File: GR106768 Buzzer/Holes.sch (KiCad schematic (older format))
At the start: 105 parts

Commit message: trying to add vias
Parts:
- H1, H10, H100, H101, H102, H103, H104, H105, H11, H12, H13, H14, H15, H16, H17, H18, H19, H2, H20, H21, H22, H23, H24, H25, H26, H27, H28, H29, H3, H30, H31, H32, H33, H34, H35, H36, H37, H38, H39, H4, H40, H41, H42, H43, H44, H45, H46, H47, H48, H49, H5, H50, H51, H52, H53, H54, H55, H56, H57, H58, H59, H6, H60, H61, H62, H63, H64, H65, H66, H67, H68, H69, H7, H70, H71, H72, H73, H74, H75, H76, H77, H78, H79, H8, H80, H81, H82, H83, H84, H85, H86, H87, H88, H89, H9, H90, H91, H92, H93, H94, H95, H96, H97, H98, H99: value Via -> GND

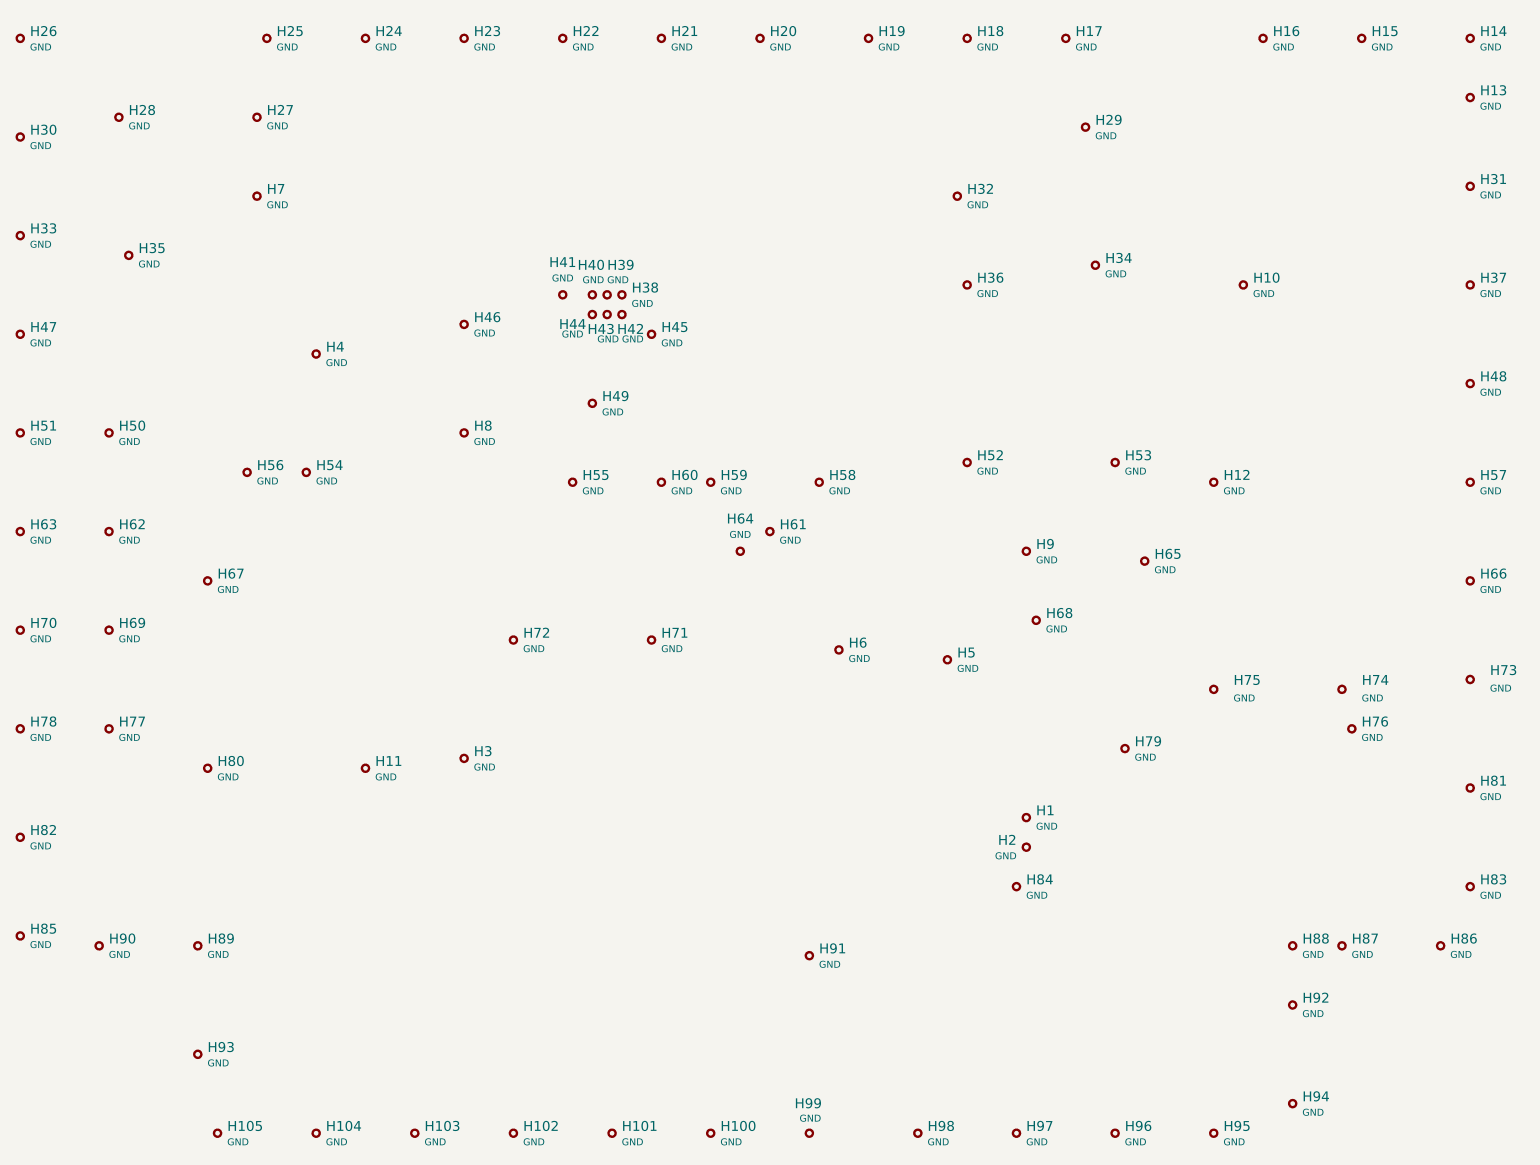
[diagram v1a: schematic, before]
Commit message: buzzer board custom via footprints
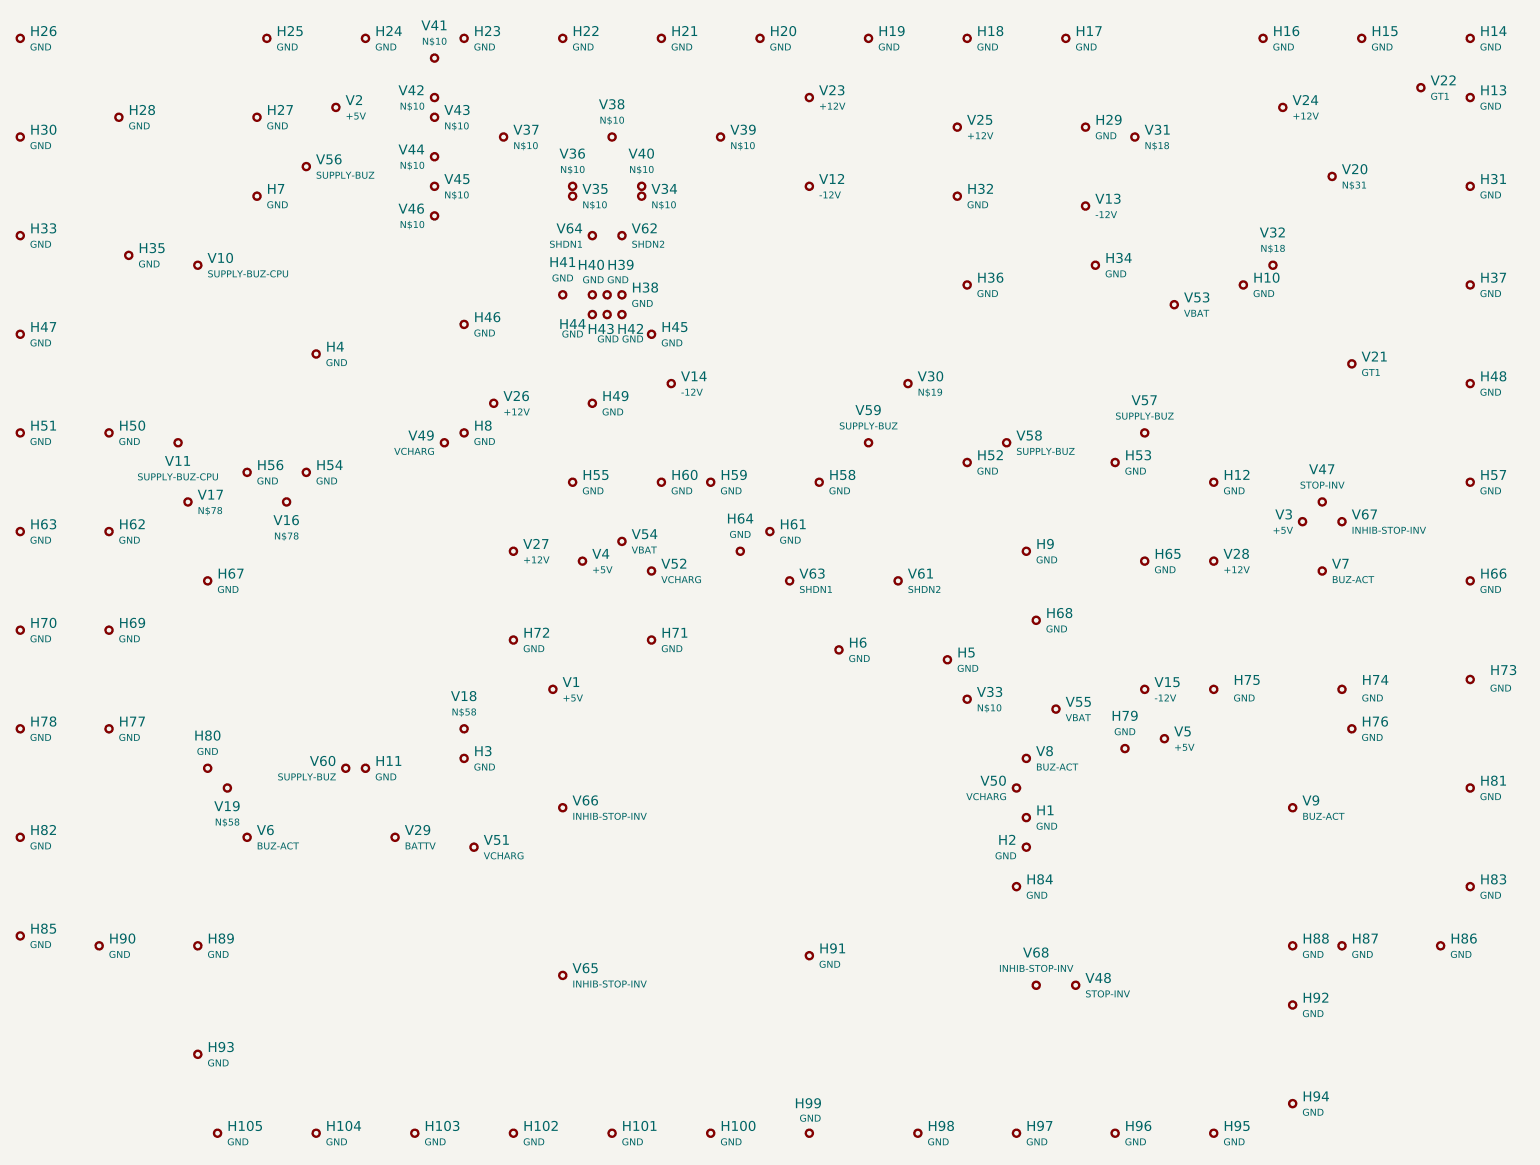
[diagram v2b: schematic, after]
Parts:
- added V1, V2, V3, V4, V5: +5V, AllModules:Via_12x32-1._.3.4, symbol GR106768_Buzzer:Via
- added V10, V11: SUPPLY-BUZ-CPU, AllModules:Via_12x32-1._.3.4, symbol GR106768_Buzzer:Via
- added V12, V13, V14, V15: -12V, AllModules:Via_12x32-1._.3.4, symbol GR106768_Buzzer:Via
- added V16, V17: N$78, AllModules:Via_12x32-1._.3.4, symbol GR106768_Buzzer:Via
- added V18, V19: N$58, AllModules:Via_12x32-1._.3.4, symbol GR106768_Buzzer:Via
- added V20: N$31, AllModules:Via_12x32-1._.3.4, symbol GR106768_Buzzer:Via
- added V21, V22: GT1, AllModules:Via_12x32-1._.3.4, symbol GR106768_Buzzer:Via
- added V23, V24, V25, V26, V27, V28: +12V, AllModules:Via_12x32-1._.3.4, symbol GR106768_Buzzer:Via
- added V29: BATTV, AllModules:Via_12x32-1._._.4, symbol GR106768_Buzzer:Via
- added V30: N$19, AllModules:Via_12x32-1._.3.4, symbol GR106768_Buzzer:Via
- added V31, V32: N$18, AllModules:Via_12x32-1._.3.4, symbol GR106768_Buzzer:Via
- added V33: N$10, AllModules:Via_12x32-1._._.4, symbol GR106768_Buzzer:Via
- added V34, V35, V36, V37, V38, V39, V40, V41, V42, V43, V44, V45, V46: N$10, AllModules:Via_12x32-1._.3.4, symbol GR106768_Buzzer:Via
- added V47, V48: STOP-INV, AllModules:Via_12x32-1._.3.4, symbol GR106768_Buzzer:Via
- added V49, V52: VCHARG, AllModules:Via_12x32-1._._.4, symbol GR106768_Buzzer:Via
- added V50, V51: VCHARG, AllModules:Via_12x32-1._.3.4, symbol GR106768_Buzzer:Via
- added V53, V54, V55: VBAT, AllModules:Via_12x32-1._.3.4, symbol GR106768_Buzzer:Via
- added V56, V57, V58, V59, V60: SUPPLY-BUZ, AllModules:Via_12x32-1._.3.4, symbol GR106768_Buzzer:Via
- added V6, V7, V8, V9: BUZ-ACT, AllModules:Via_12x32-1._.3.4, symbol GR106768_Buzzer:Via
- added V61, V62: SHDN2, AllModules:Via_12x32-1._._.4, symbol GR106768_Buzzer:Via
- added V63, V64: SHDN1, AllModules:Via_12x32-1._._.4, symbol GR106768_Buzzer:Via
- added V65, V66, V67, V68: INHIB-STOP-INV, AllModules:Via_12x32-1._.3.4, symbol GR106768_Buzzer:Via
- H1, H10, H100, H101, H102, H103, H104, H105, H11, H12, H13, H14, H15, H16, H17, H18, H19, H2, H20, H21, H22, H23, H24, H25, H26, H27, H28, H29, H3, H30, H31, H32, H33, H34, H35, H36, H37, H38, H39, H4, H40, H41, H42, H43, H44, H45, H46, H47, H48, H49, H5, H50, H51, H52, H53, H54, H55, H56, H57, H58, H59, H6, H60, H61, H62, H63, H64, H65, H66, H67, H68, H69, H7, H70, H71, H72, H73, H74, H75, H76, H77, H78, H79, H8, H80, H81, H82, H83, H84, H85, H86, H87, H88, H89, H9, H90, H91, H92, H93, H94, H95, H96, H97, H98, H99: footprint AllModules:ThroughHole_60milx12mil_Pad_Cu_Mask -> AllModules:Via_12x32
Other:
- moved on the sheet: H11

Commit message: Added Via from Buzzer board to Mechanical.lib
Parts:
- H1, H10, H100, H101, H102, H103, H104, H105, H11, H12, H13, H14, H15, H16, H17, H18, H19, H2, H20, H21, H22, H23, H24, H25, H26, H27, H28, H29, H3, H30, H31, H32, H33, H34, H35, H36, H37, H38, H39, H4, H40, H41, H42, H43, H44, H45, H46, H47, H48, H49, H5, H50, H51, H52, H53, H54, H55, H56, H57, H58, H59, H6, H60, H61, H62, H63, H64, H65, H66, H67, H68, H69, H7, H70, H71, H72, H73, H74, H75, H76, H77, H78, H79, H8, H80, H81, H82, H83, H84, H85, H86, H87, H88, H89, H9, H90, H91, H92, H93, H94, H95, H96, H97, H98, H99, V1, V10, V11, V12, V13, V14, V15, V16, V17, V18, V19, V2, V20, V21, V22, V23, V24, V25, V26, V27, V28, V29, V3, V30, V31, V32, V33, V34, V35, V36, V37, V38, V39, V4, V40, V41, V42, V43, V44, V45, V46, V47, V48, V49, V5, V50, V51, V52, V53, V54, V55, V56, V57, V58, V59, V6, V60, V61, V62, V63, V64, V65, V66, V67, V68, V7, V8, V9: symbol GR106768_Buzzer:Via -> V_Mechanical:Via

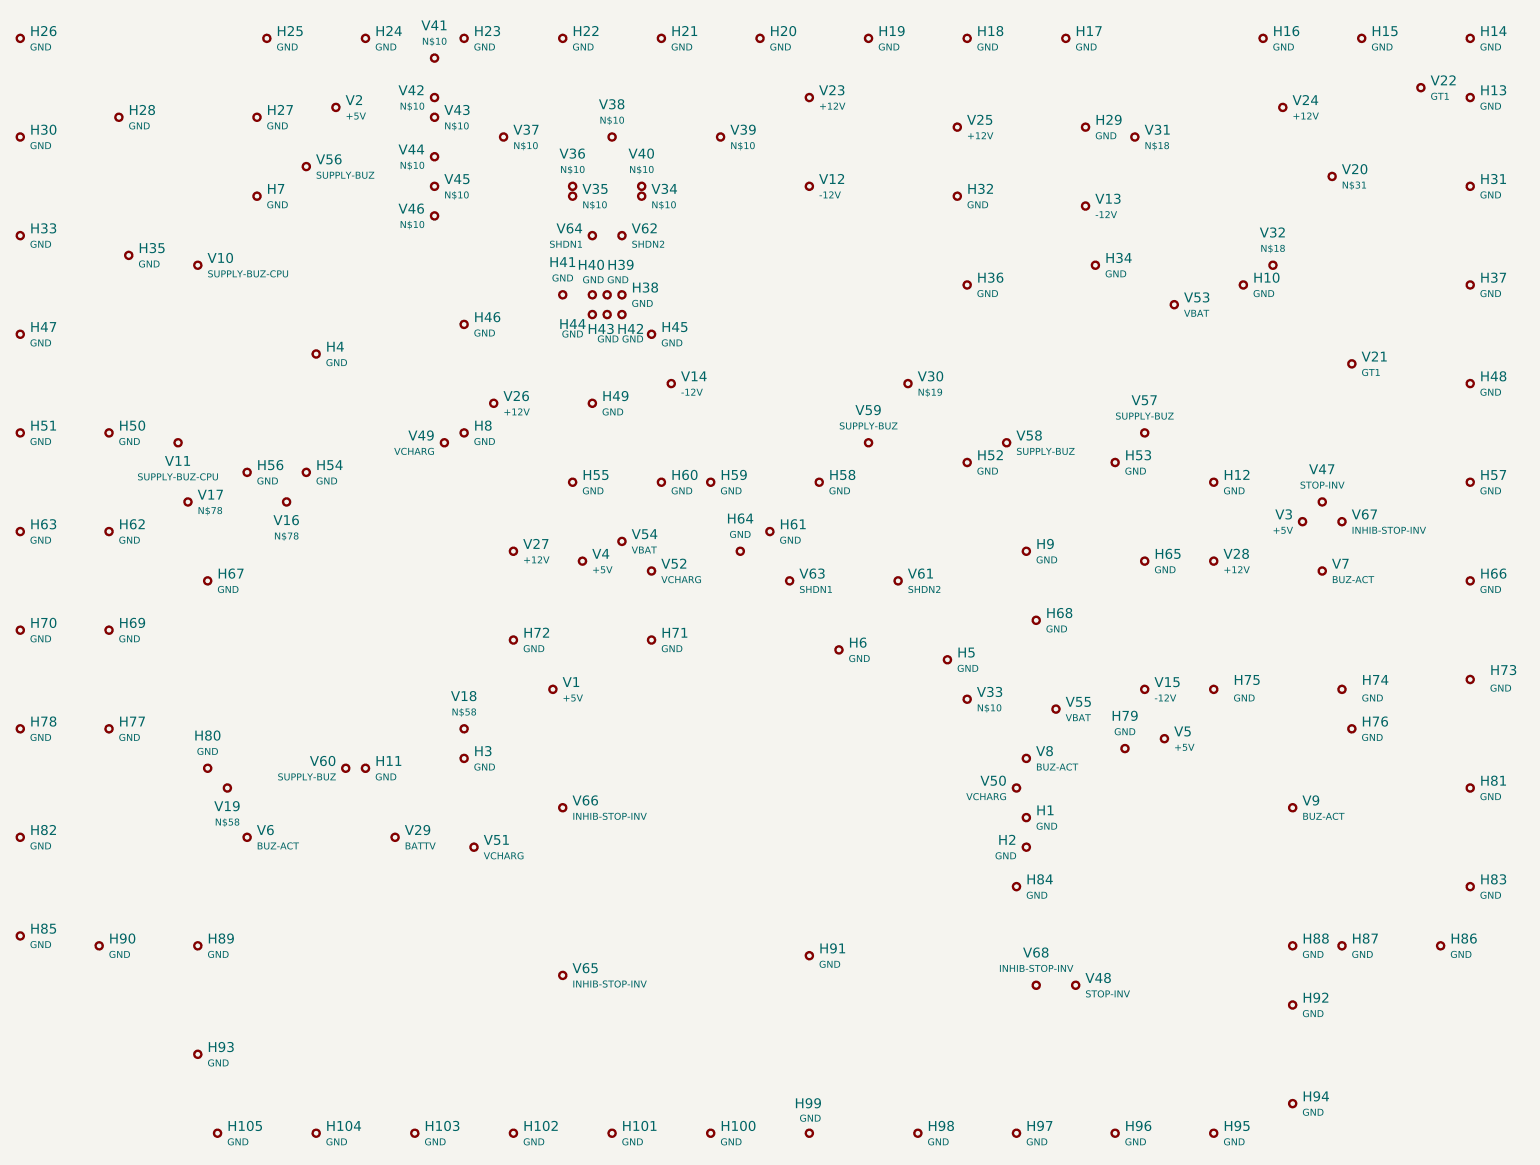
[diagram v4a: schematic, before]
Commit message: buzzer PCB updated, started on vias
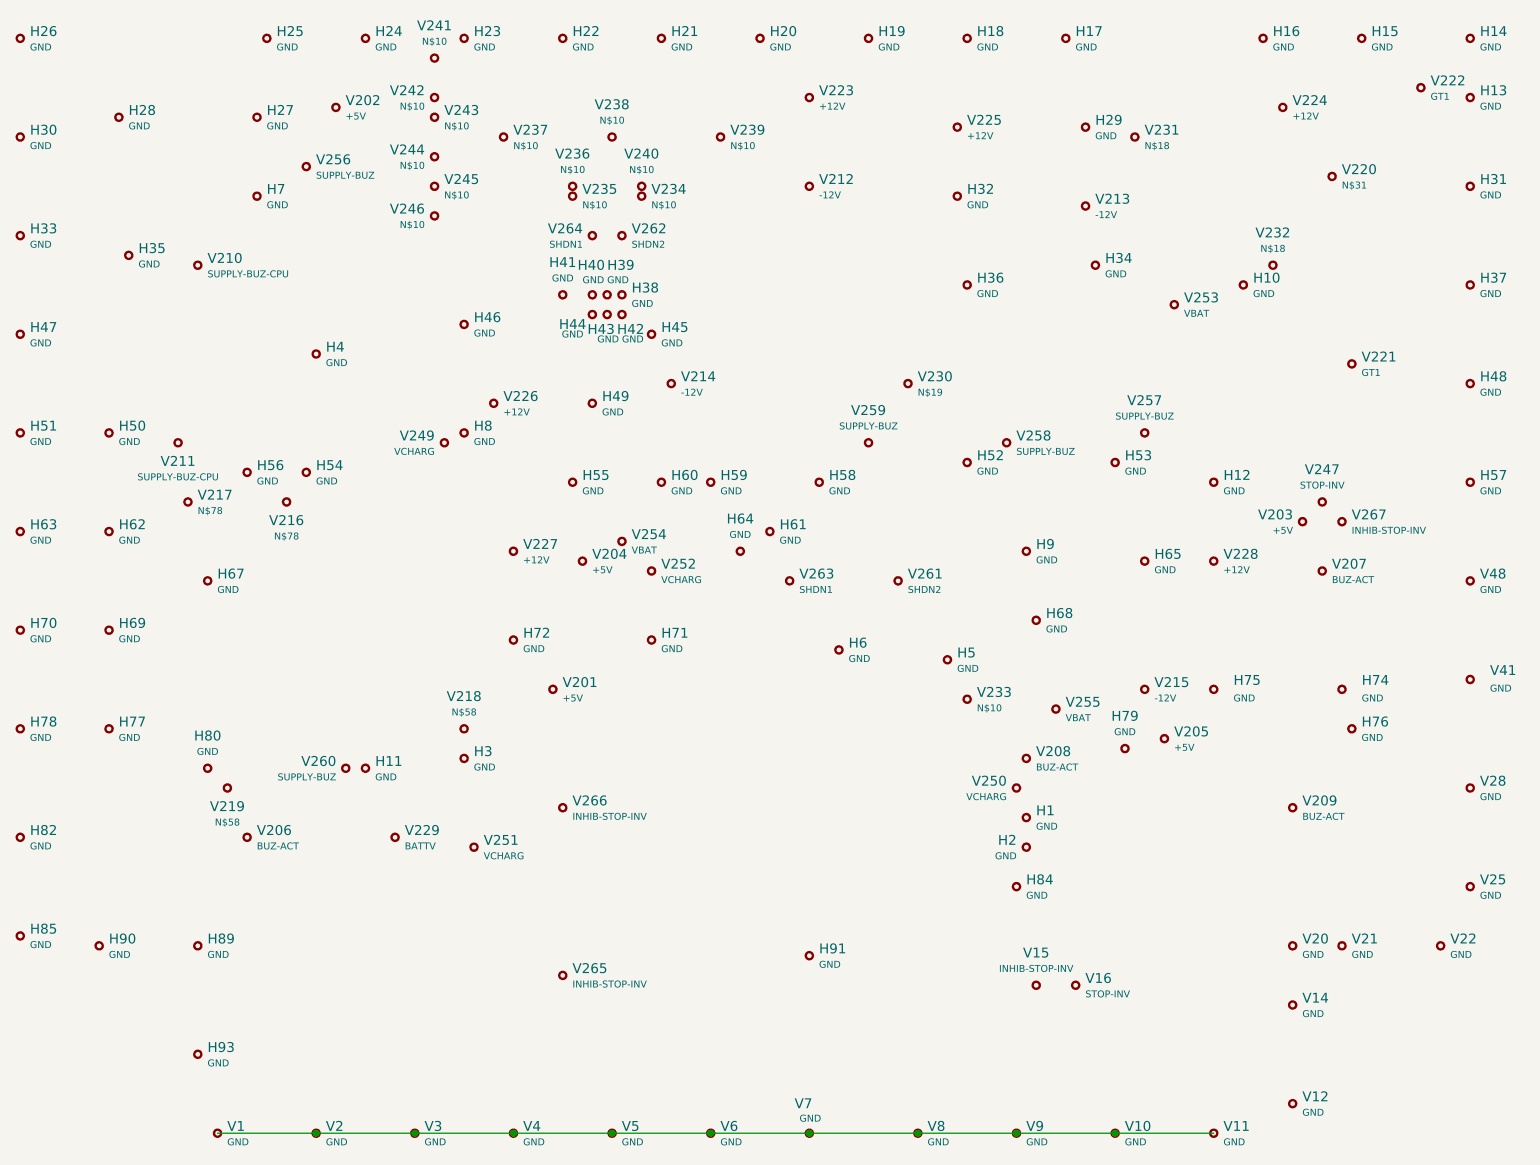
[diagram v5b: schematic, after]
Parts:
- renumbered H105 to V1, H96 to V10, H95 to V11, H94 to V12, H92 to V14, V68 to V15, V48 to V16, H104 to V2, H88 to V20, V1 to V201, V2 to V202, V3 to V203, V4 to V204, V5 to V205, V6 to V206, V7 to V207, V8 to V208, V9 to V209, H87 to V21, V10 to V210, V11 to V211, V12 to V212, V13 to V213, V14 to V214, V15 to V215, V16 to V216, V17 to V217, V18 to V218, V19 to V219, H86 to V22, V20 to V220, V21 to V221, V22 to V222, V23 to V223, V24 to V224, V25 to V225, V26 to V226, V27 to V227, V28 to V228, V29 to V229, V30 to V230, V31 to V231, V32 to V232, V33 to V233, V34 to V234, V35 to V235, V36 to V236, V37 to V237, V38 to V238, V39 to V239, V40 to V240, V41 to V241, V42 to V242, V43 to V243, V44 to V244, V45 to V245, V46 to V246, V47 to V247, V49 to V249, H83 to V25, V50 to V250, V51 to V251, V52 to V252, V53 to V253, V54 to V254, V55 to V255, V56 to V256, V57 to V257, V58 to V258, V59 to V259, V60 to V260, V61 to V261, V62 to V262, V63 to V263, V64 to V264, V65 to V265, V66 to V266, V67 to V267, H81 to V28, H103 to V3, H102 to V4, H73 to V41, H66 to V48, H101 to V5, H100 to V6, H99 to V7, H98 to V8, H97 to V9
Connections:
- net at V11.1 (#): now also V1.1 (#), V10.1 (#), V2.1 (#), V3.1 (#), V4.1 (#), V5.1 (#), V6.1 (#), V7.1 (#), V8.1 (#), V9.1 (#)
